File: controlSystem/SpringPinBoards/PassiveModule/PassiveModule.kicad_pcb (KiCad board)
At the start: 2 copper layers, 17.9 x 13.3 mm, 9 parts, among them J1 Conn_01x01_Male, J2 Conn_01x01_Male, J3 Conn_01x01_Male, J4 Conn_01x01_Male, J5 Conn_01x01_Male, J6 Conn_01x01_Male, J7 Conn_02x03_Odd_Even

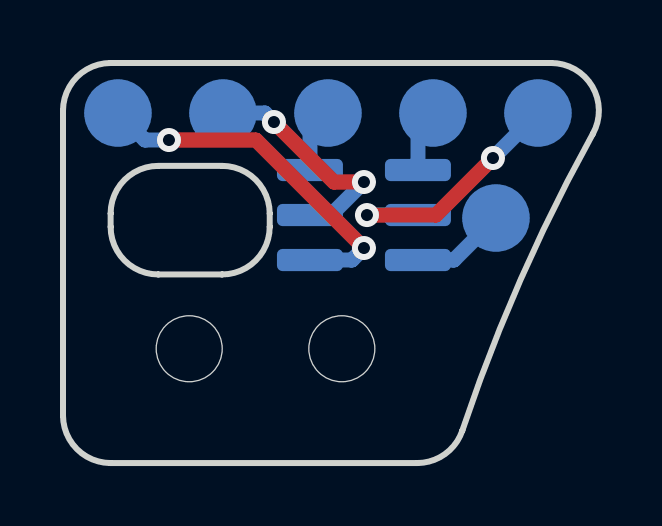
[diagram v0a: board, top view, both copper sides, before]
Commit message: Widened traces on the spring pin boards
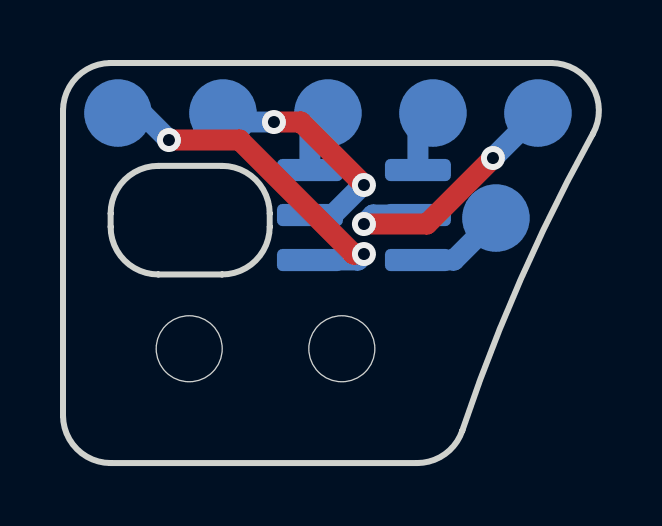
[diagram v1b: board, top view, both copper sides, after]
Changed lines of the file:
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@@
     (effects (font (size 0.5 0.5) (thickness 0.12)) (justify left mirror))
   )
-  (segment (start 176.497918 82.1) (end 173.6 82.1) (width 0.5) (layer "F.Cu") (net 1))
-  (segment (start 180.097918 85.7) (end 176.497918 82.1) (width 0.5) (layer "F.Cu") (net 1))
-  (segment (start 180.1 85.7) (end 180.097918 85.7) (width 0.5) (layer "F.Cu") (net 1))
+  (segment (start 173.6 82.1) (end 175.956497 82.1) (width 0.7) (layer "F.Cu") (net 1))
+  (segment (start 175.956497 82.1) (end 179.756497 85.9) (width 0.7) (layer "F.Cu") (net 1))
+  (segment (start 180.1 85.9) (end 180.097918 85.897918) (width 0.5) (layer "F.Cu") (net 1))
+  (segment (start 179.756497 85.9) (end 180.1 85.9) (width 0.7) (layer "F.Cu") (net 1))
   (via (at 173.6 82.1) (size 0.8) (drill 0.4) (layers "F.Cu" "B.Cu") (net 1))
-  (via (at 180.1 85.7) (size 0.8) (drill 0.4) (layers "F.Cu" "B.Cu") (net 1))
-  (segment (start 173.6 82.1) (end 172.8 82.1) (width 0.5) (layer "B.Cu") (net 1))
-  (segment (start 180.1 85.7) (end 179.7 86.1) (width 0.5) (layer "B.Cu") (net 1))
-  (segment (start 172.8 82.1) (end 171.9 81.2) (width 0.5) (layer "B.Cu") (net 1))
-  (segment (start 179.7 86.1) (end 178.3 86.1) (width 0.5) (layer "B.Cu") (net 1))
-  (segment (start 180.1 83.5) (end 179.1 83.5) (width 0.5) (layer "F.Cu") (net 2))
-  (segment (start 179.1 83.5) (end 177.1 81.5) (width 0.5) (layer "F.Cu") (net 2))
-  (via (at 180.1 83.5) (size 0.8) (drill 0.4) (layers "F.Cu" "B.Cu") (net 2))
+  (via (at 180.1 85.9) (size 0.8) (drill 0.4) (layers "F.Cu" "B.Cu") (net 1))
+  (segment (start 171.9 81.2) (end 172.7 81.2) (width 0.7) (layer "B.Cu") (net 1))
+  (segment (start 180.1 85.9) (end 179.9 86.1) (width 0.7) (layer "B.Cu") (net 1))
+  (segment (start 179.9 86.1) (end 178.3 86.1) (width 0.7) (layer "B.Cu") (net 1))
+  (segment (start 172.7 81.2) (end 173.6 82.1) (width 0.7) (layer "B.Cu") (net 1))
+  (segment (start 178 81.5) (end 180.1 83.6) (width 0.7) (layer "F.Cu") (net 2))
+  (segment (start 177.1 81.5) (end 178 81.5) (width 0.7) (layer "F.Cu") (net 2))
+  (via (at 180.1 83.6) (size 0.8) (drill 0.4) (layers "F.Cu" "B.Cu") (net 2))
   (via (at 177.1 81.5) (size 0.8) (drill 0.4) (layers "F.Cu" "B.Cu") (net 2))
-  (segment (start 180.1 83.5) (end 179 84.6) (width 0.5) (layer "B.Cu") (net 2))
-  (segment (start 176.8 81.2) (end 175.4 81.2) (width 0.5) (layer "B.Cu") (net 2))
-  (segment (start 177.1 81.5) (end 176.8 81.2) (width 0.5) (layer "B.Cu") (net 2))
-  (segment (start 179 84.6) (end 178.3 84.6) (width 0.5) (layer "B.Cu") (net 2))
-  (segment (start 178.3 81.8) (end 178.9 81.2) (width 0.5) (layer "B.Cu") (net 3))
-  (segment (start 178.3 83.1) (end 178.3 81.8) (width 0.5) (layer "B.Cu") (net 3))
-  (segment (start 181.9 81.7) (end 182.4 81.2) (width 0.5) (layer "B.Cu") (net 4))
-  (segment (start 181.9 83.1) (end 181.9 81.7) (width 0.5) (layer "B.Cu") (net 4))
-  (segment (start 182.498959 84.601041) (end 184.4 82.7) (width 0.5) (layer "F.Cu") (net 5))
-  (segment (start 180.200335 84.601041) (end 182.498959 84.601041) (width 0.5) (layer "F.Cu") (net 5))
-  (via (at 180.200335 84.601041) (size 0.8) (drill 0.4) (layers "F.Cu" "B.Cu") (net 5))
+  (segment (start 178.3 84.6) (end 179.056497 84.6) (width 0.7) (layer "B.Cu") (net 2))
+  (segment (start 175.7 81.5) (end 175.4 81.2) (width 0.7) (layer "B.Cu") (net 2))
+  (segment (start 180.056497 83.6) (end 180.1 83.6) (width 0.7) (layer "B.Cu") (net 2))
+  (segment (start 179.056497 84.6) (end 180.056497 83.6) (width 0.7) (layer "B.Cu") (net 2))
+  (segment (start 177.1 81.5) (end 175.7 81.5) (width 0.7) (layer "B.Cu") (net 2))
+  (segment (start 178.3 83.1) (end 178.3 81.8) (width 0.7) (layer "B.Cu") (net 3))
+  (segment (start 178.3 81.8) (end 178.9 81.2) (width 0.7) (layer "B.Cu") (net 3))
+  (segment (start 181.9 83.1) (end 181.9 81.7) (width 0.7) (layer "B.Cu") (net 4))
+  (segment (start 181.9 81.7) (end 182.4 81.2) (width 0.7) (layer "B.Cu") (net 4))
+  (segment (start 184.4 82.7) (end 182.2 84.9) (width 0.7) (layer "F.Cu") (net 5))
+  (segment (start 182.2 84.9) (end 180.1 84.9) (width 0.7) (layer "F.Cu") (net 5))
+  (via (at 180.1 84.9) (size 0.8) (drill 0.4) (layers "F.Cu" "B.Cu") (net 5))
   (via (at 184.4 82.7) (size 0.8) (drill 0.4) (layers "F.Cu" "B.Cu") (net 5))
-  (segment (start 184.4 82.7) (end 185.9 81.2) (width 0.5) (layer "B.Cu") (net 5))
-  (segment (start 181.9 84.6) (end 180.201376 84.6) (width 0.5) (layer "B.Cu") (net 5))
-  (segment (start 180.201376 84.6) (end 180.200335 84.601041) (width 0.5) (layer "B.Cu") (net 5))
-  (segment (start 183.1 86.1) (end 184.5 84.7) (width 0.5) (layer "B.Cu") (net 6))
-  (segment (start 181.9 86.1) (end 183.1 86.1) (width 0.5) (layer "B.Cu") (net 6))
+  (segment (start 181.9 84.6) (end 180.4 84.6) (width 0.7) (layer "B.Cu") (net 5))
+  (segment (start 184.4 82.7) (end 185.9 81.2) (width 0.7) (layer "B.Cu") (net 5))
+  (segment (start 180.4 84.6) (end 180.1 84.9) (width 0.7) (layer "B.Cu") (net 5))
+  (segment (start 181.9 86.1) (end 183.1 86.1) (width 0.7) (layer "B.Cu") (net 6))
+  (segment (start 183.1 86.1) (end 184.5 84.7) (width 0.7) (layer "B.Cu") (net 6))
 )

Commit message: Moved spring pin board libraries to psas-kicad
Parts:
- J1, J2, J3, J4, J5, J6: footprint Mill-Max-1578-3-00-15-00-00-03-0:1578-3-00-15-00-00-03-0 -> psas-footprints:Mill-Max-1578-3-00-15-00-00-03-0
- J7: footprint Wire_Pads:2x03_1.27mm_Wires_SMD -> psas-footprints:2x03_1.27mm_Wires_SMD
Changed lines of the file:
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@@
     (pad "" np_thru_hole circle (at 0 0) (size 2.2 2.2) (drill 2.2) (layers *.Cu *.Mask))
   )
-  (footprint "Mill-Max-1578-3-00-15-00-00-03-0:1578-3-00-15-00-00-03-0" (layer "B.Cu")
+  (footprint "psas-footprints:Mill-Max-1578-3-00-15-00-00-03-0" (layer "B.Cu")
     (at 184.5 84.7 180)
     (property "Sheetfile" "PassiveModule.kicad_sch")
@@
     (pad "1" smd circle (at 0 0 180) (size 2.254 2.254) (layers "B.Cu" "B.Paste" "B.Mask")
       (net 6 "Net-(J6-Pad1)") (pinfunction "Pin_1") (pintype "passive"))
-    (model "${KIPRJMOD}/mill-max-1578-3-00-15-00-00-03-0.step"
+    (model "${PSAS_LIBRARIES}/psas-3dmodels/mill-max-1578-3-00-15-00-00-03-0.step"
       (offset (xyz 0 0 0))
       (scale (xyz 1 1 1))
@@
     )
   )
-  (footprint "Mill-Max-1578-3-00-15-00-00-03-0:1578-3-00-15-00-00-03-0" (layer "B.Cu")
+  (footprint "psas-footprints:Mill-Max-1578-3-00-15-00-00-03-0" (layer "B.Cu")
     (at 175.4 81.2 180)
     (property "Sheetfile" "PassiveModule.kicad_sch")
@@
     (pad "1" smd circle (at 0 0 180) (size 2.254 2.254) (layers "B.Cu" "B.Paste" "B.Mask")
       (net 2 "Net-(J2-Pad1)") (pinfunction "Pin_1") (pintype "passive"))
-    (model "${KIPRJMOD}/mill-max-1578-3-00-15-00-00-03-0.step"
+    (model "${PSAS_LIBRARIES}/psas-3dmodels/mill-max-1578-3-00-15-00-00-03-0.step"
       (offset (xyz 0 0 0))
       (scale (xyz 1 1 1))
@@
     )
   )
-  (footprint "Wire_Pads:2x03_1.27mm_Wires_SMD" (layer "B.Cu")
+  (footprint "psas-footprints:2x03_1.27mm_Wires_SMD" (layer "B.Cu")
     (at 180.1 84.6)
     (property "Sheetfile" "PassiveModule.kicad_sch")
@@
       (net 6 "Net-(J6-Pad1)") (pinfunction "Pin_6") (pintype "passive"))
   )
-  (footprint "Mill-Max-1578-3-00-15-00-00-03-0:1578-3-00-15-00-00-03-0" (layer "B.Cu")
+  (footprint "psas-footprints:Mill-Max-1578-3-00-15-00-00-03-0" (layer "B.Cu")
     (at 178.9 81.2 180)
     (property "Sheetfile" "PassiveModule.kicad_sch")
@@
     (pad "1" smd circle (at 0 0 180) (size 2.254 2.254) (layers "B.Cu" "B.Paste" "B.Mask")
       (net 3 "Net-(J3-Pad1)") (pinfunction "Pin_1") (pintype "passive"))
-    (model "${KIPRJMOD}/mill-max-1578-3-00-15-00-00-03-0.step"
+    (model "${PSAS_LIBRARIES}/psas-3dmodels/mill-max-1578-3-00-15-00-00-03-0.step"
       (offset (xyz 0 0 0))
       (scale (xyz 1 1 1))
@@
     )
   )
-  (footprint "Mill-Max-1578-3-00-15-00-00-03-0:1578-3-00-15-00-00-03-0" (layer "B.Cu")
+  (footprint "psas-footprints:Mill-Max-1578-3-00-15-00-00-03-0" (layer "B.Cu")
     (at 171.9 81.2 180)
     (property "Sheetfile" "PassiveModule.kicad_sch")
@@
     (pad "1" smd circle (at 0 0 180) (size 2.254 2.254) (layers "B.Cu" "B.Paste" "B.Mask")
       (net 1 "Net-(J1-Pad1)") (pinfunction "Pin_1") (pintype "passive"))
-    (model "${KIPRJMOD}/mill-max-1578-3-00-15-00-00-03-0.step"
+    (model "${PSAS_LIBRARIES}/psas-3dmodels/mill-max-1578-3-00-15-00-00-03-0.step"
       (offset (xyz 0 0 0))
       (scale (xyz 1 1 1))
@@
     )
   )
-  (footprint "Mill-Max-1578-3-00-15-00-00-03-0:1578-3-00-15-00-00-03-0" (layer "B.Cu")
+  (footprint "psas-footprints:Mill-Max-1578-3-00-15-00-00-03-0" (layer "B.Cu")
     (at 185.9 81.2 180)
     (property "Sheetfile" "PassiveModule.kicad_sch")
@@
     (pad "1" smd circle (at 0 0 180) (size 2.254 2.254) (layers "B.Cu" "B.Paste" "B.Mask")
       (net 5 "Net-(J5-Pad1)") (pinfunction "Pin_1") (pintype "passive"))
-    (model "${KIPRJMOD}/mill-max-1578-3-00-15-00-00-03-0.step"
+    (model "${PSAS_LIBRARIES}/psas-3dmodels/mill-max-1578-3-00-15-00-00-03-0.step"
       (offset (xyz 0 0 0))
       (scale (xyz 1 1 1))
@@
     )
   )
-  (footprint "Mill-Max-1578-3-00-15-00-00-03-0:1578-3-00-15-00-00-03-0" (layer "B.Cu")
+  (footprint "psas-footprints:Mill-Max-1578-3-00-15-00-00-03-0" (layer "B.Cu")
     (at 182.4 81.2 180)
     (property "Sheetfile" "PassiveModule.kicad_sch")
@@
     (pad "1" smd circle (at 0 0 180) (size 2.254 2.254) (layers "B.Cu" "B.Paste" "B.Mask")
       (net 4 "Net-(J4-Pad1)") (pinfunction "Pin_1") (pintype "passive"))
-    (model "${KIPRJMOD}/mill-max-1578-3-00-15-00-00-03-0.step"
+    (model "${PSAS_LIBRARIES}/psas-3dmodels/mill-max-1578-3-00-15-00-00-03-0.step"
       (offset (xyz 0 0 0))
       (scale (xyz 1 1 1))
